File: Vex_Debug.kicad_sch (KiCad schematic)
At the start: 40 parts, among them J1 USB_C_Receptacle_USB2.0, J2 Micro_SD_Card, J3 Conn_01x02_Pin, Q1 BC817, Q2 BC817, U1 ESP32-C3-WROOM-02-N4, U2 NCP1117-3.3_SOT223, U3 ADM3493ARZ, U4 FT231XQ

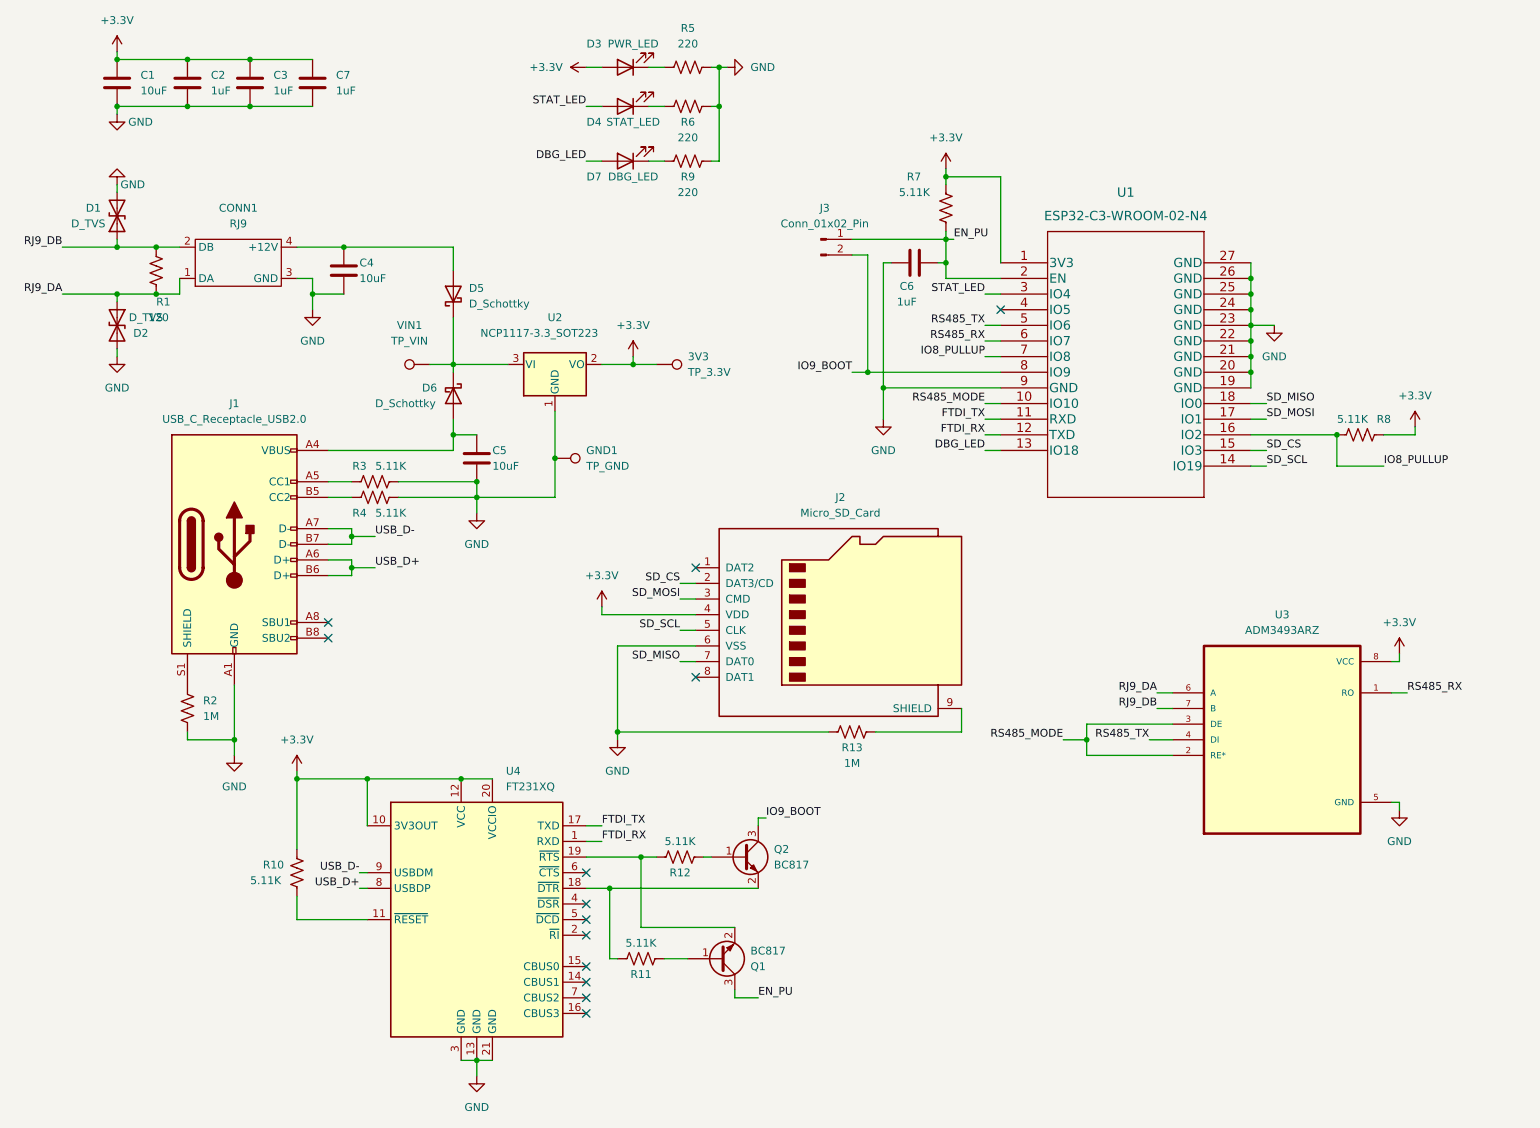
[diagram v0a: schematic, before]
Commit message: we no longer gonna use esp32
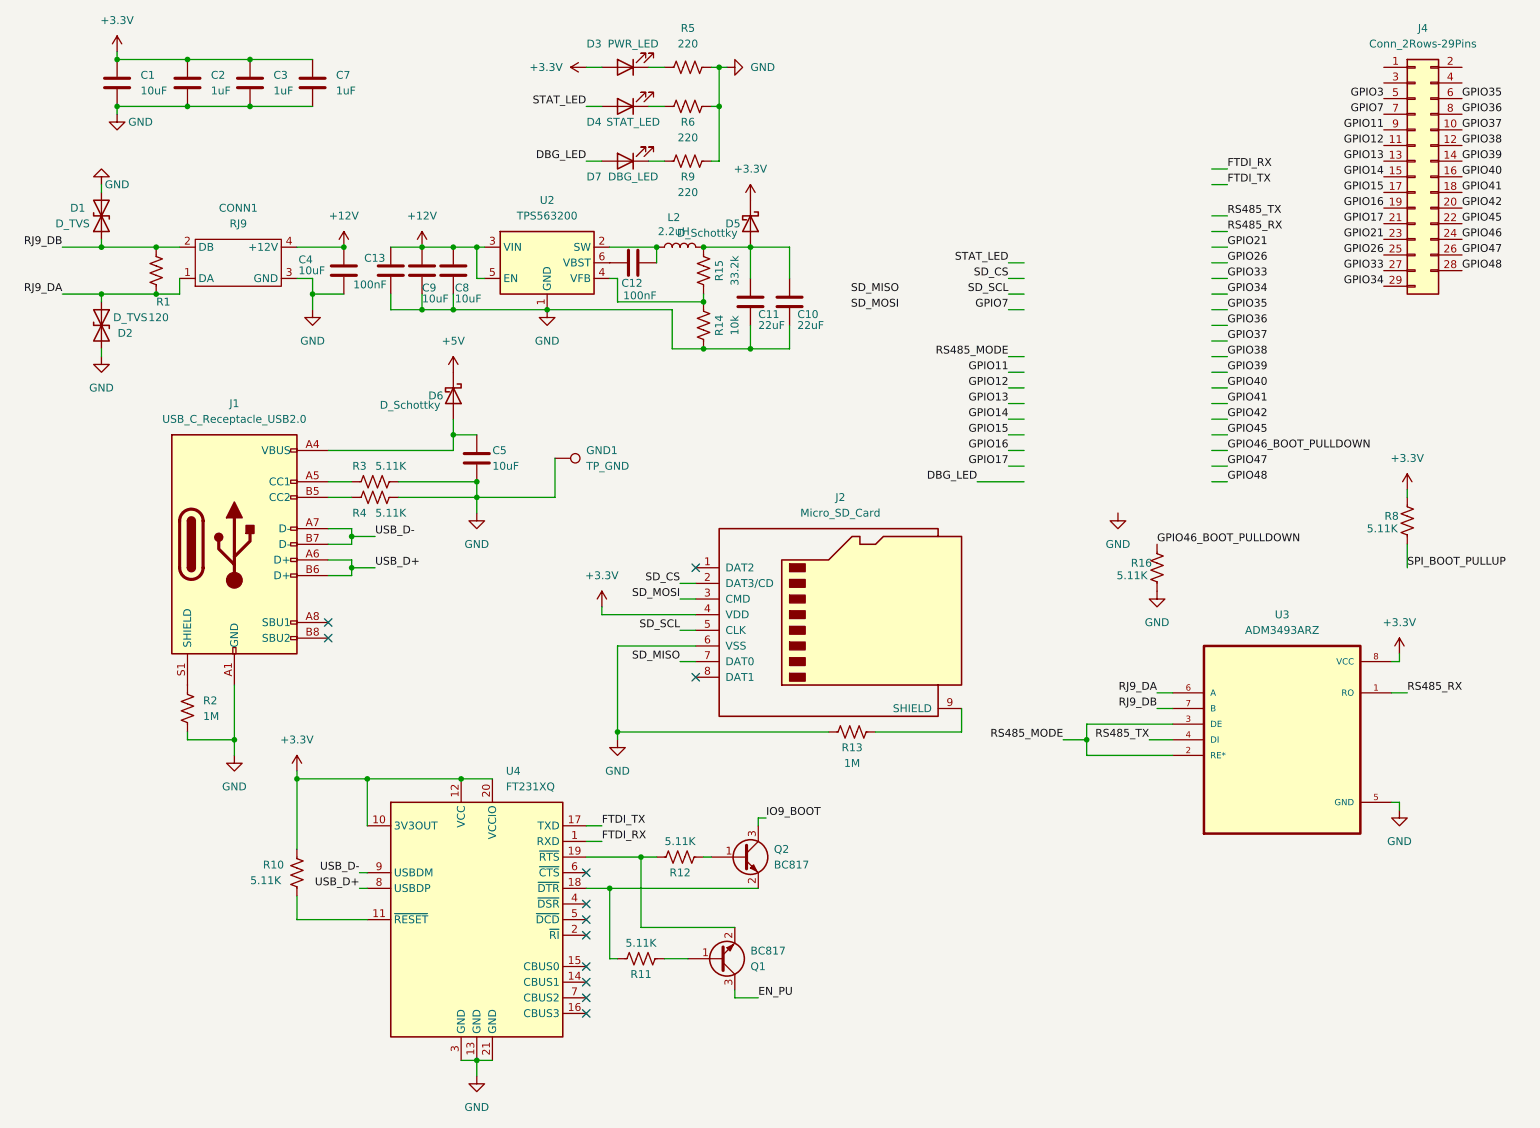
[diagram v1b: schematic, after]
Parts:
- removed 3V3: TP_3.3V, TestPoint:TestPoint_Pad_D1.5mm, symbol Connector:TestPoint
- removed C6: 1uF, Capacitor_SMD:C_0805_2012Metric_Pad1.18x1.45mm_HandSolder, symbol Device:C
- removed J3: Conn_01x02_Pin, Connector_PinHeader_2.54mm:PinHeader_1x02_P2.54mm_Vertical, symbol Connector:Conn_01x02_Pin
- removed R7: 5.11K, Resistor_SMD:R_0805_2012Metric_Pad1.20x1.40mm_HandSolder, symbol Device:R_US
- removed U1: ESP32-C3-WROOM-02-N4, ESP32-C3-WROOM:ESP32-C3-WROOM-02-N4, symbol ESP32-C3-WROOM:ESP32-C3-WROOM-02-N4
- removed U2: NCP1117-3.3_SOT223, Package_TO_SOT_SMD:SOT-223-3_TabPin2, symbol Regulator_Linear:NCP1117-3.3_SOT223
- removed VIN1: TP_VIN, TestPoint:TestPoint_Pad_D1.5mm, symbol Connector:TestPoint
- added C10, C11: 22uF, Capacitor_SMD:C_0805_2012Metric_Pad1.18x1.45mm_HandSolder, symbol Device:C
- added C12, C13: 100nF, Capacitor_SMD:C_0805_2012Metric_Pad1.18x1.45mm_HandSolder, symbol Device:C
- added C8, C9: 10uF, Capacitor_SMD:C_0805_2012Metric_Pad1.18x1.45mm_HandSolder, symbol Device:C
- added J4: Conn_2Rows-29Pins, symbol Connector_Generic:Conn_2Rows-29Pins
- added L2: 2.2uH, symbol Device:L
- added R14: 10k, Resistor_SMD:R_0805_2012Metric_Pad1.20x1.40mm_HandSolder, symbol Device:R_US
- added R15: 33.2k, Resistor_SMD:R_0805_2012Metric_Pad1.20x1.40mm_HandSolder, symbol Device:R_US
- added R16: 5.11K, Resistor_SMD:R_0805_2012Metric_Pad1.20x1.40mm_HandSolder, symbol Device:R_US
- added U2: TPS563200, Package_TO_SOT_SMD:SOT-23-6, symbol Regulator_Switching:TPS563200
- D5, D6: footprint Diode_SMD:D_SOD-323_HandSoldering -> (none)
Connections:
- net +3.3V: now also D5.1 (K)
- net GND: now also C10.2, C11.2, C13.2, C8.2, C9.2, R14.1, R16.1, U2.1 (GND)
- net +5V: now reaches D6.1 (K)
- net +5V: no longer D5.1 (K)
- net +12V: now reaches C4.1, CONN1.4 (+12V)
- net +12V: now also C13.1, C8.1, C9.1, U2.3 (VIN), U2.5 (EN); no longer D5.2 (A)
- net IO8_PULLUP renamed SPI_BOOT_PULLUP
- new net: R14.2, R15.1, U2.4 (VFB)
- new net: C10.1, C11.1, D5.2 (A), L2.2, R15.2
- new net: C12.2, L2.1, U2.2 (SW)
- new net: C12.1, U2.6 (VBST)
- new net GPIO11: J4.9 (Pin_9)
- new net GPIO12: J4.11 (Pin_11)
- new net GPIO13: J4.13 (Pin_13)
- new net GPIO14: J4.15 (Pin_15)
- new net GPIO15: J4.17 (Pin_17)
- new net GPIO16: J4.19 (Pin_19)
- new net GPIO17: J4.21 (Pin_21)
- new net GPIO21: J4.23 (Pin_23)
- new net GPIO26: J4.25 (Pin_25)
- new net GPIO3: J4.5 (Pin_5)
- new net GPIO33: J4.27 (Pin_27)
- new net GPIO34: J4.29 (Pin_29)
- new net GPIO35: J4.6 (Pin_6)
- new net GPIO36: J4.8 (Pin_8)
- new net GPIO37: J4.10 (Pin_10)
- new net GPIO38: J4.12 (Pin_12)
- new net GPIO39: J4.14 (Pin_14)
- new net GPIO40: J4.16 (Pin_16)
- new net GPIO41: J4.18 (Pin_18)
- new net GPIO42: J4.20 (Pin_20)
- new net GPIO45: J4.22 (Pin_22)
- new net GPIO46: J4.24 (Pin_24)
- new net GPIO46_BOOT_PULLDOWN: R16.2
- new net GPIO47: J4.26 (Pin_26)
- new net GPIO48: J4.28 (Pin_28)
- new net GPIO7: J4.7 (Pin_7)
- no-connect marks 13 -> 12
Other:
- moved on the sheet: D1, D2, R8
